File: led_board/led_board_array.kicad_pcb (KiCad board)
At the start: 2 copper layers, 87.6 x 84 mm, 144 parts, among them J1 Conn_01x03, J2 Conn_01x02, J3 Conn_01x02, J4 Conn_01x02

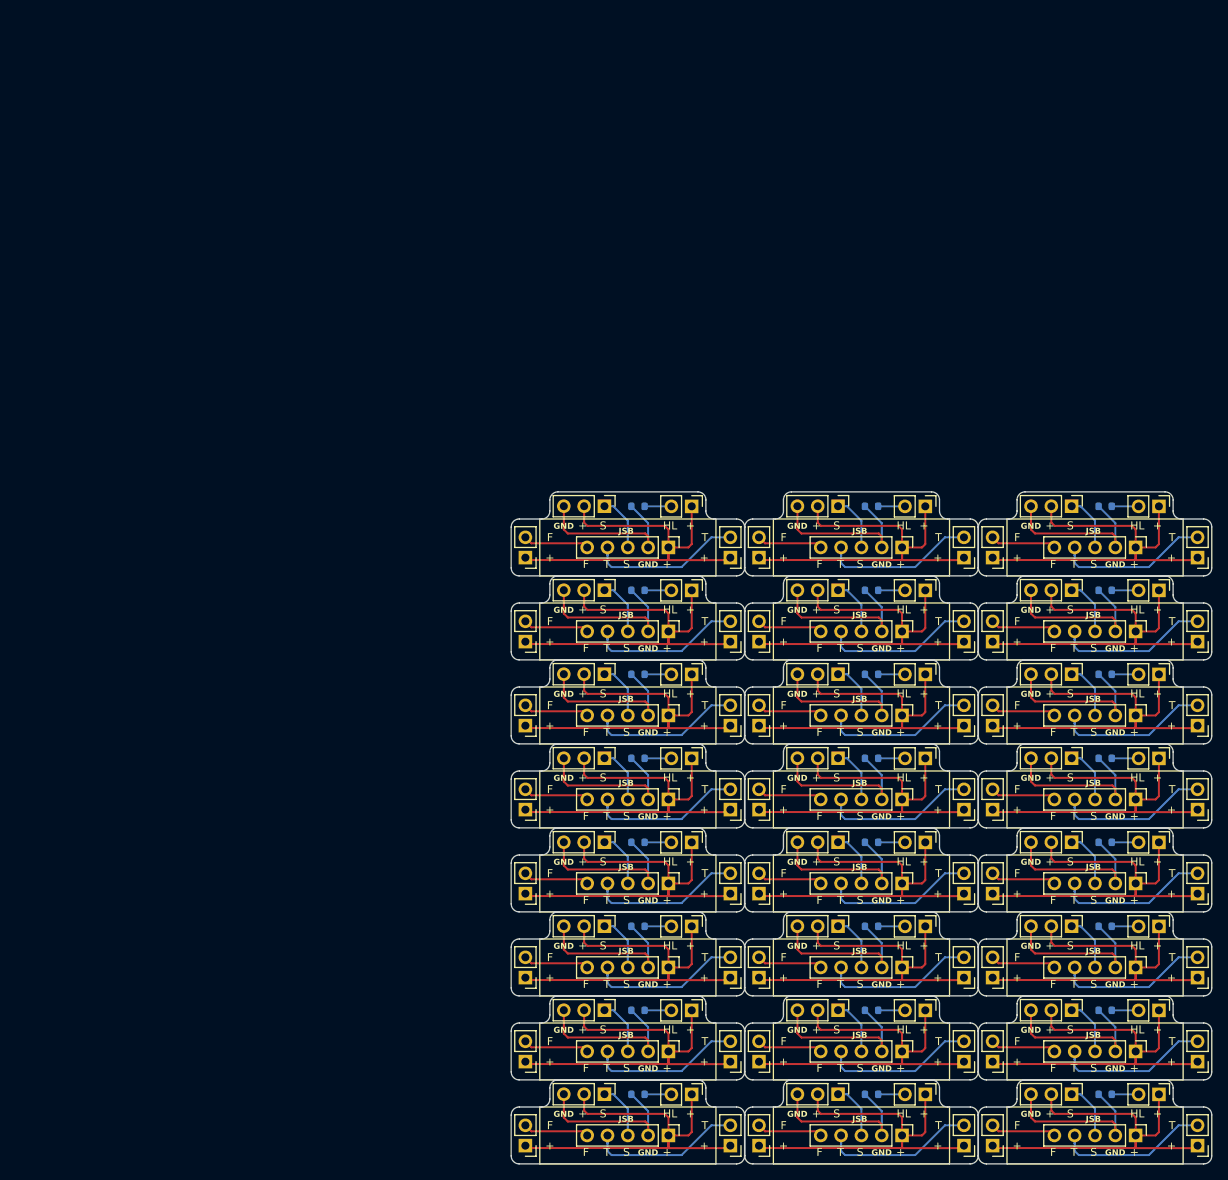
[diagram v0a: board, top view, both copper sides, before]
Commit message: feat: modify logo
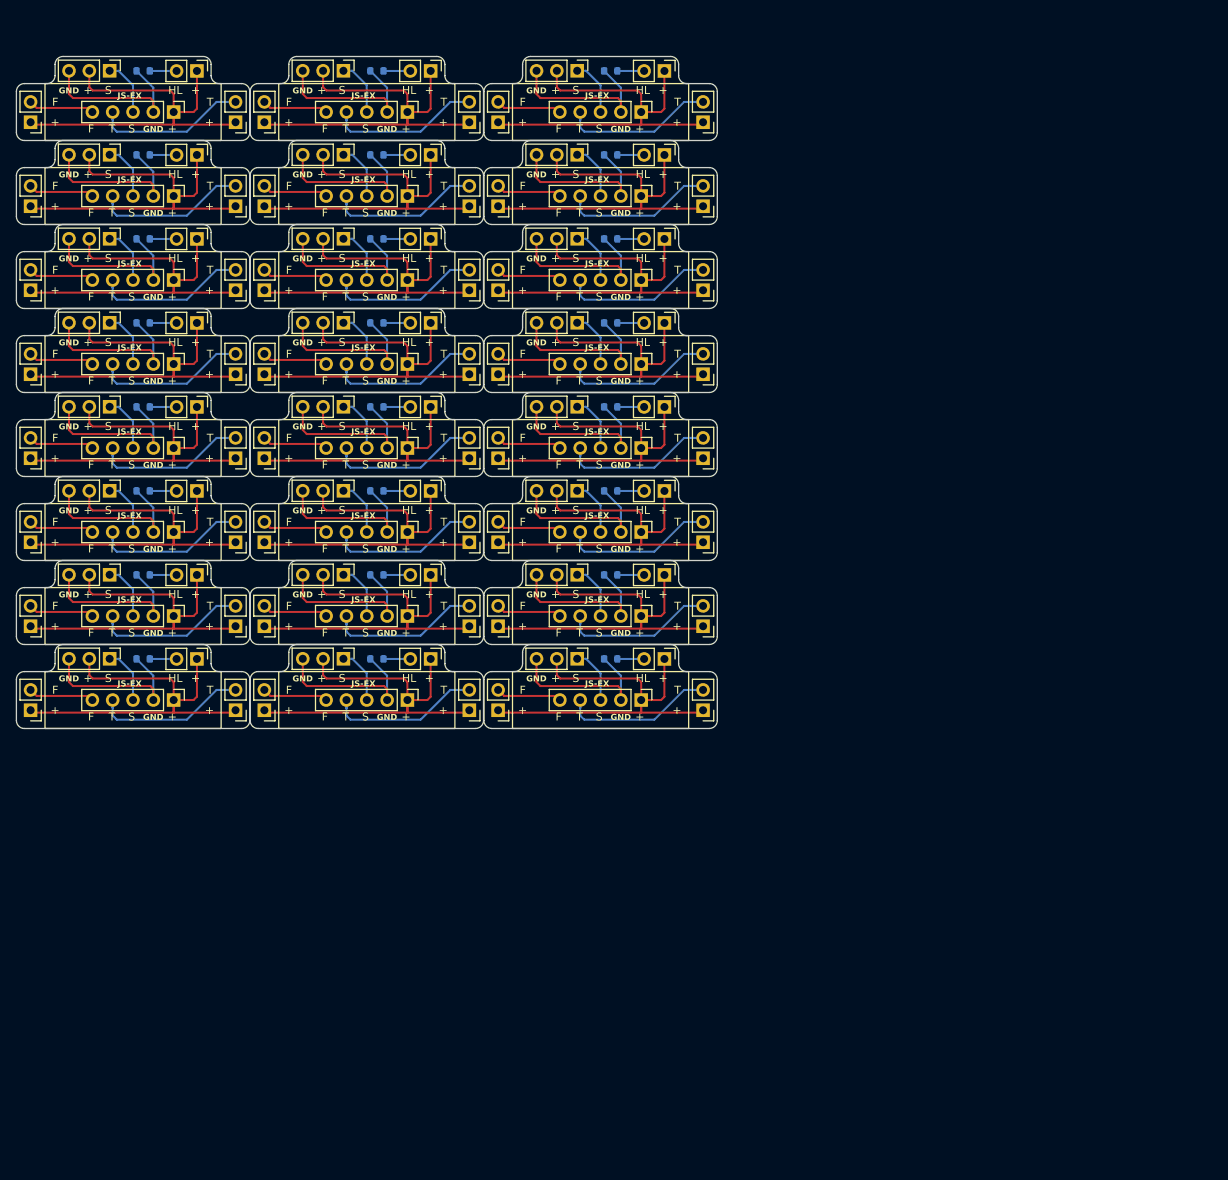
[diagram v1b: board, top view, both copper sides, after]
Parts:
- removed the J1 at (139.3, 150.9)
- removed the J1 at (110.1, 171.9)
- removed the J1 at (168.5, 108.9)
- removed the J1 at (168.5, 171.9)
- removed the J1 at (110.1, 161.4)
- removed the J1 at (110.1, 129.9)
- removed the J1 at (110.1, 98.4)
- removed the J1 at (110.1, 108.9)
- removed the J1 at (139.3, 171.9)
- removed the J1 at (168.5, 129.9)
- removed the J1 at (168.5, 150.9)
- removed the J1 at (110.1, 150.9)
- removed the J1 at (168.5, 140.4)
- removed the J1 at (110.1, 140.4)
- removed the J1 at (139.3, 129.9)
- removed the J1 at (139.3, 108.9)
- removed the J1 at (110.1, 119.4)
- removed the J1 at (139.3, 119.4)
- removed the J1 at (139.3, 98.4)
- removed the J1 at (139.3, 161.4)
- removed the J1 at (168.5, 161.4)
- removed the J1 at (168.5, 98.4)
- removed the J1 at (168.5, 119.4)
- removed the J1 at (139.3, 140.4)
- removed the J2 at (121.0, 140.4)
- removed the J2 at (121.0, 161.4)
- removed the J2 at (121.0, 108.9)
- removed the J2 at (150.2, 150.9)
- removed the J2 at (179.4, 171.9)
- removed the J2 at (150.2, 140.4)
- removed the J2 at (179.4, 119.4)
- removed the J2 at (121.0, 119.4)
- removed the J2 at (121.0, 129.9)
- removed the J2 at (121.0, 150.9)
- removed the J2 at (150.2, 98.4)
- removed the J2 at (179.4, 129.9)
- removed the J2 at (150.2, 161.4)
- removed the J2 at (150.2, 171.9)
- removed the J2 at (179.4, 161.4)
- removed the J2 at (179.4, 98.4)
- removed the J2 at (121.0, 171.9)
- removed the J2 at (121.0, 98.4)
- removed the J2 at (179.4, 140.4)
- removed the J2 at (150.2, 119.4)
- removed the J2 at (179.4, 108.9)
- removed the J2 at (179.4, 150.9)
- removed the J2 at (150.2, 129.9)
- removed the J2 at (150.2, 108.9)
- removed the J3 at (100.2, 136.3)
- removed the J3 at (158.6, 136.3)
- removed the J3 at (129.4, 157.3)
- removed the J3 at (158.6, 125.8)
- removed the J3 at (129.4, 167.8)
- removed the J3 at (158.6, 167.8)
- removed the J3 at (100.2, 167.8)
- removed the J3 at (100.2, 146.8)
- removed the J3 at (129.4, 104.8)
- removed the J3 at (158.6, 157.3)
- removed the J3 at (158.6, 146.8)
- removed the J3 at (129.4, 178.3)
- removed the J3 at (158.6, 104.8)
- removed the J3 at (129.4, 125.8)
- removed the J3 at (100.2, 157.3)
- removed the J3 at (129.4, 115.3)
- removed the J3 at (129.4, 146.8)
- removed the J3 at (158.6, 115.3)
- removed the J3 at (158.6, 178.3)
- removed the J3 at (100.2, 125.8)
- removed the J3 at (100.2, 115.3)
- removed the J3 at (100.2, 178.3)
- removed the J3 at (100.2, 104.8)
- removed the J3 at (129.4, 136.3)
- removed the J4 at (155.0, 146.8)
- removed the J4 at (155.0, 104.8)
- removed the J4 at (184.2, 115.3)
- removed the J4 at (125.8, 104.8)
- removed the J4 at (125.8, 178.3)
- removed the J4 at (125.8, 125.8)
- removed the J4 at (184.2, 178.3)
- removed the J4 at (155.0, 178.3)
- removed the J4 at (125.8, 115.3)
- removed the J4 at (184.2, 104.8)
- removed the J4 at (184.2, 157.3)
- removed the J4 at (155.0, 167.8)
- removed the J4 at (125.8, 157.3)
- removed the J4 at (155.0, 115.3)
- removed the J4 at (155.0, 157.3)
- removed the J4 at (184.2, 167.8)
- removed the J4 at (125.8, 146.8)
- removed the J4 at (125.8, 136.3)
- removed the J4 at (155.0, 125.8)
- removed the J4 at (184.2, 146.8)
- removed the J4 at (184.2, 136.3)
- removed the J4 at (125.8, 167.8)
- removed the J4 at (155.0, 136.3)
- removed the J4 at (184.2, 125.8)
- removed the JSB1 at (118.1, 135.1)
- removed the JSB1 at (118.1, 156.1)
- removed the JSB1 at (118.1, 177.1)
- removed the JSB1 at (118.1, 124.6)
- removed the JSB1 at (176.5, 135.1)
- removed the JSB1 at (147.3, 156.1)
- removed the JSB1 at (118.1, 145.6)
- removed the JSB1 at (176.5, 156.1)
- removed the JSB1 at (147.3, 166.6)
- removed the JSB1 at (118.1, 114.1)
- removed the JSB1 at (176.5, 114.1)
- removed the JSB1 at (147.3, 124.6)
- removed the JSB1 at (176.5, 177.1)
- removed the JSB1 at (147.3, 177.1)
- removed the JSB1 at (118.1, 166.6)
- removed the JSB1 at (147.3, 103.6)
- removed the JSB1 at (147.3, 135.1)
- removed the JSB1 at (147.3, 114.1)
- removed the JSB1 at (176.5, 103.6)
- removed the JSB1 at (176.5, 124.6)
- removed the JSB1 at (176.5, 145.6)
- removed the JSB1 at (147.3, 145.6)
- removed the JSB1 at (176.5, 166.6)
- removed the JSB1 at (118.1, 103.6)
- removed the R1 at (172.7, 119.4)
- removed the R1 at (172.7, 140.4)
- removed the R1 at (172.7, 171.9)
- removed the R1 at (114.3, 171.9)
- removed the R1 at (143.5, 108.9)
- removed the R1 at (114.3, 119.4)
- removed the R1 at (114.3, 161.4)
- removed the R1 at (172.7, 108.9)
- removed the R1 at (114.3, 140.4)
- removed the R1 at (172.7, 98.4)
- removed the R1 at (143.5, 129.9)
- removed the R1 at (114.3, 129.9)
- removed the R1 at (143.5, 161.4)
- removed the R1 at (143.5, 119.4)
- removed the R1 at (143.5, 140.4)
- removed the R1 at (143.5, 98.4)
- removed the R1 at (143.5, 150.9)
- removed the R1 at (143.5, 171.9)
- removed the R1 at (172.7, 150.9)
- removed the R1 at (172.7, 161.4)
- removed the R1 at (114.3, 108.9)
- removed the R1 at (172.7, 129.9)
- removed the R1 at (114.3, 150.9)
- removed the R1 at (114.3, 98.4)
- added J1: Conn_01x03, Connector_PinHeader_2.54mm:PinHeader_1x03_P2.54mm_Vertical, F.Cu at (48.2, 44.0)
- added J1: Conn_01x03, Connector_PinHeader_2.54mm:PinHeader_1x03_P2.54mm_Vertical, F.Cu at (48.2, 117.5)
- added J1: Conn_01x03, Connector_PinHeader_2.54mm:PinHeader_1x03_P2.54mm_Vertical, F.Cu at (48.2, 75.5)
- added J1: Conn_01x03, Connector_PinHeader_2.54mm:PinHeader_1x03_P2.54mm_Vertical, F.Cu at (106.7, 65.0)
- added J1: Conn_01x03, Connector_PinHeader_2.54mm:PinHeader_1x03_P2.54mm_Vertical, F.Cu at (77.5, 54.5)
- added J1: Conn_01x03, Connector_PinHeader_2.54mm:PinHeader_1x03_P2.54mm_Vertical, F.Cu at (48.2, 54.5)
- added J1: Conn_01x03, Connector_PinHeader_2.54mm:PinHeader_1x03_P2.54mm_Vertical, F.Cu at (106.7, 44.0)
- added J1: Conn_01x03, Connector_PinHeader_2.54mm:PinHeader_1x03_P2.54mm_Vertical, F.Cu at (106.7, 96.5)
- added J1: Conn_01x03, Connector_PinHeader_2.54mm:PinHeader_1x03_P2.54mm_Vertical, F.Cu at (48.2, 65.0)
- added J1: Conn_01x03, Connector_PinHeader_2.54mm:PinHeader_1x03_P2.54mm_Vertical, F.Cu at (77.5, 117.5)
- added J1: Conn_01x03, Connector_PinHeader_2.54mm:PinHeader_1x03_P2.54mm_Vertical, F.Cu at (106.7, 54.5)
- added J1: Conn_01x03, Connector_PinHeader_2.54mm:PinHeader_1x03_P2.54mm_Vertical, F.Cu at (48.2, 107.0)
- added J1: Conn_01x03, Connector_PinHeader_2.54mm:PinHeader_1x03_P2.54mm_Vertical, F.Cu at (77.5, 96.5)
- added J1: Conn_01x03, Connector_PinHeader_2.54mm:PinHeader_1x03_P2.54mm_Vertical, F.Cu at (106.7, 107.0)
- added J1: Conn_01x03, Connector_PinHeader_2.54mm:PinHeader_1x03_P2.54mm_Vertical, F.Cu at (48.2, 96.5)
- added J1: Conn_01x03, Connector_PinHeader_2.54mm:PinHeader_1x03_P2.54mm_Vertical, F.Cu at (77.5, 75.5)
- added J1: Conn_01x03, Connector_PinHeader_2.54mm:PinHeader_1x03_P2.54mm_Vertical, F.Cu at (77.5, 86.0)
- added J1: Conn_01x03, Connector_PinHeader_2.54mm:PinHeader_1x03_P2.54mm_Vertical, F.Cu at (77.5, 107.0)
- added J1: Conn_01x03, Connector_PinHeader_2.54mm:PinHeader_1x03_P2.54mm_Vertical, F.Cu at (77.5, 65.0)
- added J1: Conn_01x03, Connector_PinHeader_2.54mm:PinHeader_1x03_P2.54mm_Vertical, F.Cu at (106.7, 117.5)
- added J1: Conn_01x03, Connector_PinHeader_2.54mm:PinHeader_1x03_P2.54mm_Vertical, F.Cu at (77.5, 44.0)
- added J1: Conn_01x03, Connector_PinHeader_2.54mm:PinHeader_1x03_P2.54mm_Vertical, F.Cu at (106.7, 86.0)
- added J1: Conn_01x03, Connector_PinHeader_2.54mm:PinHeader_1x03_P2.54mm_Vertical, F.Cu at (106.7, 75.5)
- added J1: Conn_01x03, Connector_PinHeader_2.54mm:PinHeader_1x03_P2.54mm_Vertical, F.Cu at (48.2, 86.0)
- added J2: Conn_01x02, Connector_PinHeader_2.54mm:PinHeader_1x02_P2.54mm_Vertical, F.Cu at (59.1, 65.0)
- added J2: Conn_01x02, Connector_PinHeader_2.54mm:PinHeader_1x02_P2.54mm_Vertical, F.Cu at (88.4, 44.0)
- added J2: Conn_01x02, Connector_PinHeader_2.54mm:PinHeader_1x02_P2.54mm_Vertical, F.Cu at (117.6, 65.0)
- added J2: Conn_01x02, Connector_PinHeader_2.54mm:PinHeader_1x02_P2.54mm_Vertical, F.Cu at (59.1, 117.5)
- added J2: Conn_01x02, Connector_PinHeader_2.54mm:PinHeader_1x02_P2.54mm_Vertical, F.Cu at (117.6, 107.0)
- added J2: Conn_01x02, Connector_PinHeader_2.54mm:PinHeader_1x02_P2.54mm_Vertical, F.Cu at (117.6, 44.0)
- added J2: Conn_01x02, Connector_PinHeader_2.54mm:PinHeader_1x02_P2.54mm_Vertical, F.Cu at (88.4, 107.0)
- added J2: Conn_01x02, Connector_PinHeader_2.54mm:PinHeader_1x02_P2.54mm_Vertical, F.Cu at (59.1, 44.0)
- added J2: Conn_01x02, Connector_PinHeader_2.54mm:PinHeader_1x02_P2.54mm_Vertical, F.Cu at (88.4, 75.5)
- added J2: Conn_01x02, Connector_PinHeader_2.54mm:PinHeader_1x02_P2.54mm_Vertical, F.Cu at (88.4, 117.5)
- added J2: Conn_01x02, Connector_PinHeader_2.54mm:PinHeader_1x02_P2.54mm_Vertical, F.Cu at (88.4, 96.5)
- added J2: Conn_01x02, Connector_PinHeader_2.54mm:PinHeader_1x02_P2.54mm_Vertical, F.Cu at (88.4, 54.5)
- added J2: Conn_01x02, Connector_PinHeader_2.54mm:PinHeader_1x02_P2.54mm_Vertical, F.Cu at (59.1, 107.0)
- added J2: Conn_01x02, Connector_PinHeader_2.54mm:PinHeader_1x02_P2.54mm_Vertical, F.Cu at (117.6, 117.5)
- added J2: Conn_01x02, Connector_PinHeader_2.54mm:PinHeader_1x02_P2.54mm_Vertical, F.Cu at (117.6, 75.5)
- added J2: Conn_01x02, Connector_PinHeader_2.54mm:PinHeader_1x02_P2.54mm_Vertical, F.Cu at (59.1, 96.5)
- added J2: Conn_01x02, Connector_PinHeader_2.54mm:PinHeader_1x02_P2.54mm_Vertical, F.Cu at (117.6, 86.0)
- added J2: Conn_01x02, Connector_PinHeader_2.54mm:PinHeader_1x02_P2.54mm_Vertical, F.Cu at (88.4, 65.0)
- added J2: Conn_01x02, Connector_PinHeader_2.54mm:PinHeader_1x02_P2.54mm_Vertical, F.Cu at (117.6, 96.5)
- added J2: Conn_01x02, Connector_PinHeader_2.54mm:PinHeader_1x02_P2.54mm_Vertical, F.Cu at (117.6, 54.5)
- added J2: Conn_01x02, Connector_PinHeader_2.54mm:PinHeader_1x02_P2.54mm_Vertical, F.Cu at (88.4, 86.0)
- added J2: Conn_01x02, Connector_PinHeader_2.54mm:PinHeader_1x02_P2.54mm_Vertical, F.Cu at (59.1, 75.5)
- added J2: Conn_01x02, Connector_PinHeader_2.54mm:PinHeader_1x02_P2.54mm_Vertical, F.Cu at (59.1, 54.5)
- added J2: Conn_01x02, Connector_PinHeader_2.54mm:PinHeader_1x02_P2.54mm_Vertical, F.Cu at (59.1, 86.0)
- added J3: Conn_01x02, Connector_PinHeader_2.54mm:PinHeader_1x02_P2.54mm_Vertical, F.Cu at (96.8, 113.4)
- added J3: Conn_01x02, Connector_PinHeader_2.54mm:PinHeader_1x02_P2.54mm_Vertical, F.Cu at (38.4, 71.4)
- added J3: Conn_01x02, Connector_PinHeader_2.54mm:PinHeader_1x02_P2.54mm_Vertical, F.Cu at (96.8, 102.9)
- added J3: Conn_01x02, Connector_PinHeader_2.54mm:PinHeader_1x02_P2.54mm_Vertical, F.Cu at (67.6, 123.9)
- added J3: Conn_01x02, Connector_PinHeader_2.54mm:PinHeader_1x02_P2.54mm_Vertical, F.Cu at (96.8, 92.4)
- added J3: Conn_01x02, Connector_PinHeader_2.54mm:PinHeader_1x02_P2.54mm_Vertical, F.Cu at (67.6, 71.4)
- added J3: Conn_01x02, Connector_PinHeader_2.54mm:PinHeader_1x02_P2.54mm_Vertical, F.Cu at (96.8, 81.9)
- added J3: Conn_01x02, Connector_PinHeader_2.54mm:PinHeader_1x02_P2.54mm_Vertical, F.Cu at (67.6, 92.4)
- added J3: Conn_01x02, Connector_PinHeader_2.54mm:PinHeader_1x02_P2.54mm_Vertical, F.Cu at (67.6, 81.9)
- added J3: Conn_01x02, Connector_PinHeader_2.54mm:PinHeader_1x02_P2.54mm_Vertical, F.Cu at (38.4, 92.4)
- added J3: Conn_01x02, Connector_PinHeader_2.54mm:PinHeader_1x02_P2.54mm_Vertical, F.Cu at (96.8, 123.9)
- added J3: Conn_01x02, Connector_PinHeader_2.54mm:PinHeader_1x02_P2.54mm_Vertical, F.Cu at (67.6, 60.9)
- added J3: Conn_01x02, Connector_PinHeader_2.54mm:PinHeader_1x02_P2.54mm_Vertical, F.Cu at (67.6, 113.4)
- added J3: Conn_01x02, Connector_PinHeader_2.54mm:PinHeader_1x02_P2.54mm_Vertical, F.Cu at (38.4, 102.9)
- added J3: Conn_01x02, Connector_PinHeader_2.54mm:PinHeader_1x02_P2.54mm_Vertical, F.Cu at (96.8, 50.4)
- added J3: Conn_01x02, Connector_PinHeader_2.54mm:PinHeader_1x02_P2.54mm_Vertical, F.Cu at (67.6, 102.9)
- added J3: Conn_01x02, Connector_PinHeader_2.54mm:PinHeader_1x02_P2.54mm_Vertical, F.Cu at (38.4, 113.4)
- added J3: Conn_01x02, Connector_PinHeader_2.54mm:PinHeader_1x02_P2.54mm_Vertical, F.Cu at (96.8, 71.4)
- added J3: Conn_01x02, Connector_PinHeader_2.54mm:PinHeader_1x02_P2.54mm_Vertical, F.Cu at (67.6, 50.4)
- added J3: Conn_01x02, Connector_PinHeader_2.54mm:PinHeader_1x02_P2.54mm_Vertical, F.Cu at (96.8, 60.9)
- added J3: Conn_01x02, Connector_PinHeader_2.54mm:PinHeader_1x02_P2.54mm_Vertical, F.Cu at (38.4, 123.9)
- added J3: Conn_01x02, Connector_PinHeader_2.54mm:PinHeader_1x02_P2.54mm_Vertical, F.Cu at (38.4, 50.4)
- added J3: Conn_01x02, Connector_PinHeader_2.54mm:PinHeader_1x02_P2.54mm_Vertical, F.Cu at (38.4, 81.9)
- added J3: Conn_01x02, Connector_PinHeader_2.54mm:PinHeader_1x02_P2.54mm_Vertical, F.Cu at (38.4, 60.9)
- added J4: Conn_01x02, Connector_PinHeader_2.54mm:PinHeader_1x02_P2.54mm_Vertical, F.Cu at (122.4, 81.9)
- added J4: Conn_01x02, Connector_PinHeader_2.54mm:PinHeader_1x02_P2.54mm_Vertical, F.Cu at (122.4, 71.4)
- added J4: Conn_01x02, Connector_PinHeader_2.54mm:PinHeader_1x02_P2.54mm_Vertical, F.Cu at (64.0, 123.9)
- added J4: Conn_01x02, Connector_PinHeader_2.54mm:PinHeader_1x02_P2.54mm_Vertical, F.Cu at (122.4, 50.4)
- added J4: Conn_01x02, Connector_PinHeader_2.54mm:PinHeader_1x02_P2.54mm_Vertical, F.Cu at (93.2, 123.9)
- added J4: Conn_01x02, Connector_PinHeader_2.54mm:PinHeader_1x02_P2.54mm_Vertical, F.Cu at (64.0, 102.9)
- added J4: Conn_01x02, Connector_PinHeader_2.54mm:PinHeader_1x02_P2.54mm_Vertical, F.Cu at (93.2, 71.4)
- added J4: Conn_01x02, Connector_PinHeader_2.54mm:PinHeader_1x02_P2.54mm_Vertical, F.Cu at (64.0, 60.9)
- added J4: Conn_01x02, Connector_PinHeader_2.54mm:PinHeader_1x02_P2.54mm_Vertical, F.Cu at (122.4, 92.4)
- added J4: Conn_01x02, Connector_PinHeader_2.54mm:PinHeader_1x02_P2.54mm_Vertical, F.Cu at (93.2, 50.4)
- added J4: Conn_01x02, Connector_PinHeader_2.54mm:PinHeader_1x02_P2.54mm_Vertical, F.Cu at (122.4, 60.9)
- added J4: Conn_01x02, Connector_PinHeader_2.54mm:PinHeader_1x02_P2.54mm_Vertical, F.Cu at (122.4, 102.9)
- added J4: Conn_01x02, Connector_PinHeader_2.54mm:PinHeader_1x02_P2.54mm_Vertical, F.Cu at (93.2, 113.4)
- added J4: Conn_01x02, Connector_PinHeader_2.54mm:PinHeader_1x02_P2.54mm_Vertical, F.Cu at (122.4, 113.4)
- added J4: Conn_01x02, Connector_PinHeader_2.54mm:PinHeader_1x02_P2.54mm_Vertical, F.Cu at (64.0, 71.4)
- added J4: Conn_01x02, Connector_PinHeader_2.54mm:PinHeader_1x02_P2.54mm_Vertical, F.Cu at (64.0, 113.4)
- added J4: Conn_01x02, Connector_PinHeader_2.54mm:PinHeader_1x02_P2.54mm_Vertical, F.Cu at (64.0, 92.4)
- added J4: Conn_01x02, Connector_PinHeader_2.54mm:PinHeader_1x02_P2.54mm_Vertical, F.Cu at (64.0, 50.4)
- added J4: Conn_01x02, Connector_PinHeader_2.54mm:PinHeader_1x02_P2.54mm_Vertical, F.Cu at (93.2, 92.4)
- added J4: Conn_01x02, Connector_PinHeader_2.54mm:PinHeader_1x02_P2.54mm_Vertical, F.Cu at (93.2, 81.9)
- added J4: Conn_01x02, Connector_PinHeader_2.54mm:PinHeader_1x02_P2.54mm_Vertical, F.Cu at (93.2, 60.9)
- added J4: Conn_01x02, Connector_PinHeader_2.54mm:PinHeader_1x02_P2.54mm_Vertical, F.Cu at (64.0, 81.9)
- added J4: Conn_01x02, Connector_PinHeader_2.54mm:PinHeader_1x02_P2.54mm_Vertical, F.Cu at (93.2, 102.9)
- added J4: Conn_01x02, Connector_PinHeader_2.54mm:PinHeader_1x02_P2.54mm_Vertical, F.Cu at (122.4, 123.9)
- added JSB1: Conn_01x05, Connector_PinHeader_2.54mm:PinHeader_1x05_P2.54mm_Vertical, F.Cu at (114.7, 59.6)
- added JSB1: Conn_01x05, Connector_PinHeader_2.54mm:PinHeader_1x05_P2.54mm_Vertical, F.Cu at (85.5, 101.6)
- added JSB1: Conn_01x05, Connector_PinHeader_2.54mm:PinHeader_1x05_P2.54mm_Vertical, F.Cu at (114.7, 91.1)
- added JSB1: Conn_01x05, Connector_PinHeader_2.54mm:PinHeader_1x05_P2.54mm_Vertical, F.Cu at (85.5, 122.6)
- added JSB1: Conn_01x05, Connector_PinHeader_2.54mm:PinHeader_1x05_P2.54mm_Vertical, F.Cu at (85.5, 70.1)
- added JSB1: Conn_01x05, Connector_PinHeader_2.54mm:PinHeader_1x05_P2.54mm_Vertical, F.Cu at (56.2, 112.1)
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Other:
- outline, holes or cut-outs redrawn
- board text added: "JS-EX"
- board text removed: "JSB"

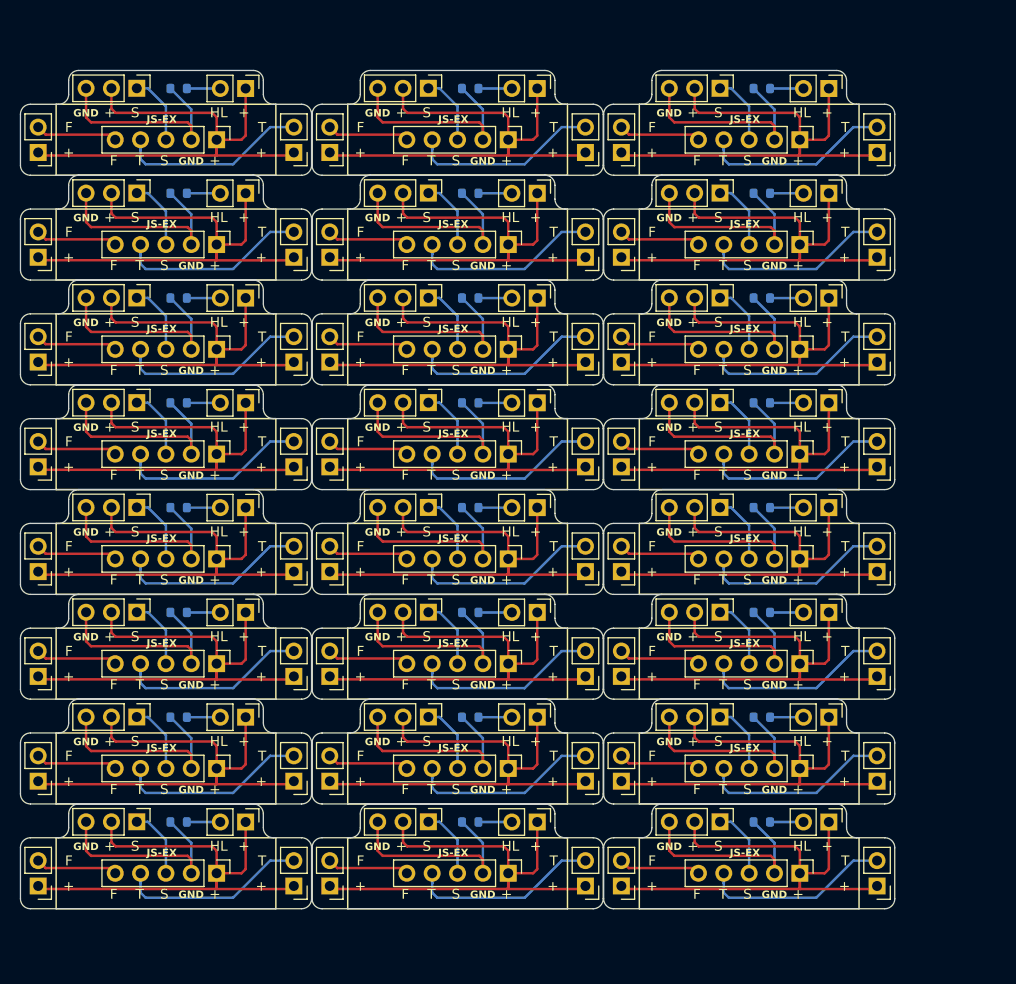
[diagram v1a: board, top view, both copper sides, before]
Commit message: feat(led_board): update array
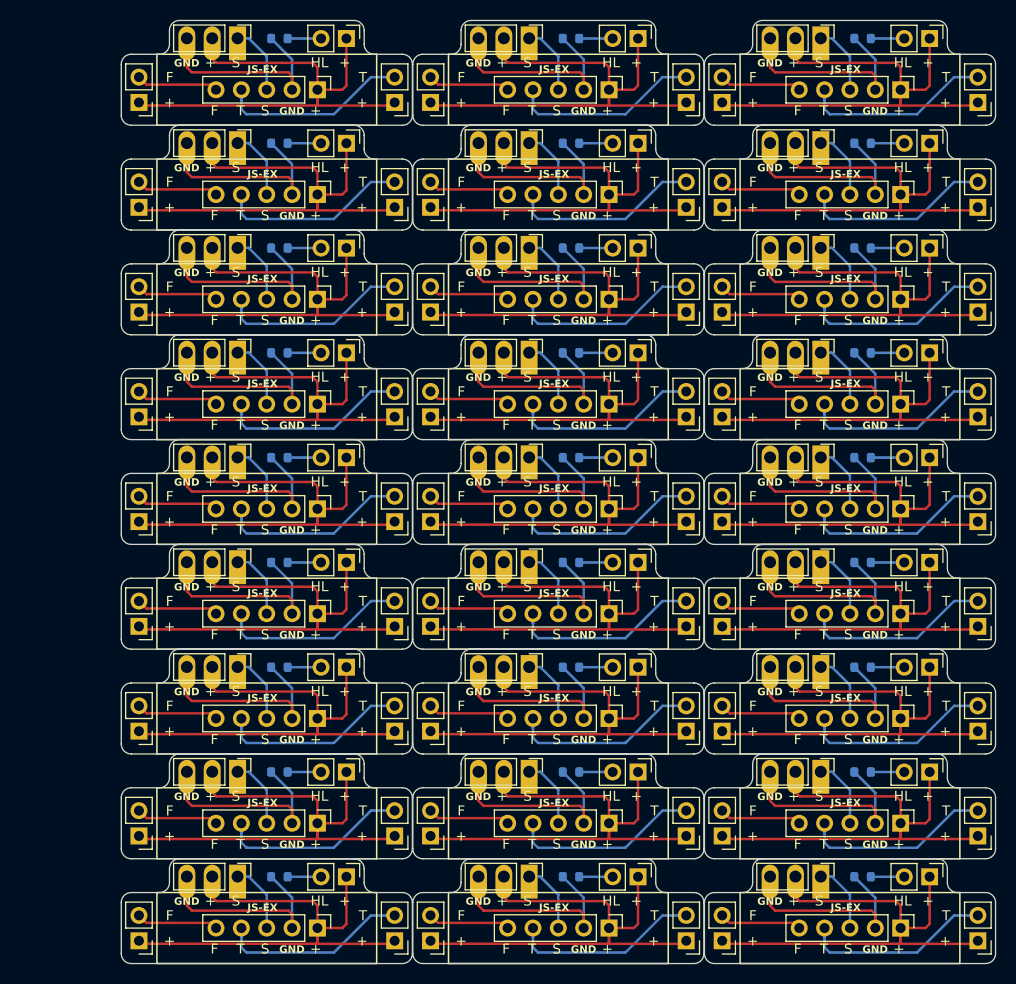
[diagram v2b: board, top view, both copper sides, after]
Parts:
- removed the J1 at (48.2, 44.0)
- removed the J1 at (48.2, 117.5)
- removed the J1 at (48.2, 75.5)
- removed the J1 at (106.7, 65.0)
- removed the J1 at (77.5, 54.5)
- removed the J1 at (48.2, 54.5)
- removed the J1 at (106.7, 44.0)
- removed the J1 at (106.7, 96.5)
- removed the J1 at (48.2, 65.0)
- removed the J1 at (77.5, 117.5)
- removed the J1 at (106.7, 54.5)
- removed the J1 at (48.2, 107.0)
- removed the J1 at (77.5, 96.5)
- removed the J1 at (106.7, 107.0)
- removed the J1 at (48.2, 96.5)
- removed the J1 at (77.5, 75.5)
- removed the J1 at (77.5, 86.0)
- removed the J1 at (77.5, 107.0)
- removed the J1 at (77.5, 65.0)
- removed the J1 at (106.7, 117.5)
- removed the J1 at (77.5, 44.0)
- removed the J1 at (106.7, 86.0)
- removed the J1 at (106.7, 75.5)
- removed the J1 at (48.2, 86.0)
- removed the J2 at (59.1, 65.0)
- removed the J2 at (88.4, 44.0)
- removed the J2 at (117.6, 65.0)
- removed the J2 at (59.1, 117.5)
- removed the J2 at (117.6, 107.0)
- removed the J2 at (117.6, 44.0)
- removed the J2 at (88.4, 107.0)
- removed the J2 at (59.1, 44.0)
- removed the J2 at (88.4, 75.5)
- removed the J2 at (88.4, 117.5)
- removed the J2 at (88.4, 96.5)
- removed the J2 at (88.4, 54.5)
- removed the J2 at (59.1, 107.0)
- removed the J2 at (117.6, 117.5)
- removed the J2 at (117.6, 75.5)
- removed the J2 at (59.1, 96.5)
- removed the J2 at (117.6, 86.0)
- removed the J2 at (88.4, 65.0)
- removed the J2 at (117.6, 96.5)
- removed the J2 at (117.6, 54.5)
- removed the J2 at (88.4, 86.0)
- removed the J2 at (59.1, 75.5)
- removed the J2 at (59.1, 54.5)
- removed the J2 at (59.1, 86.0)
- removed the J3 at (96.8, 113.4)
- removed the J3 at (38.4, 71.4)
- removed the J3 at (96.8, 102.9)
- removed the J3 at (67.6, 123.9)
- removed the J3 at (96.8, 92.4)
- removed the J3 at (67.6, 71.4)
- removed the J3 at (96.8, 81.9)
- removed the J3 at (67.6, 92.4)
- removed the J3 at (67.6, 81.9)
- removed the J3 at (38.4, 92.4)
- removed the J3 at (96.8, 123.9)
- removed the J3 at (67.6, 60.9)
- removed the J3 at (67.6, 113.4)
- removed the J3 at (38.4, 102.9)
- removed the J3 at (96.8, 50.4)
- removed the J3 at (67.6, 102.9)
- removed the J3 at (38.4, 113.4)
- removed the J3 at (96.8, 71.4)
- removed the J3 at (67.6, 50.4)
- removed the J3 at (96.8, 60.9)
- removed the J3 at (38.4, 123.9)
- removed the J3 at (38.4, 50.4)
- removed the J3 at (38.4, 81.9)
- removed the J3 at (38.4, 60.9)
- removed the J4 at (122.4, 81.9)
- removed the J4 at (122.4, 71.4)
- removed the J4 at (64.0, 123.9)
- removed the J4 at (122.4, 50.4)
- removed the J4 at (93.2, 123.9)
- removed the J4 at (64.0, 102.9)
- removed the J4 at (93.2, 71.4)
- removed the J4 at (64.0, 60.9)
- removed the J4 at (122.4, 92.4)
- removed the J4 at (93.2, 50.4)
- removed the J4 at (122.4, 60.9)
- removed the J4 at (122.4, 102.9)
- removed the J4 at (93.2, 113.4)
- removed the J4 at (122.4, 113.4)
- removed the J4 at (64.0, 71.4)
- removed the J4 at (64.0, 113.4)
- removed the J4 at (64.0, 92.4)
- removed the J4 at (64.0, 50.4)
- removed the J4 at (93.2, 92.4)
- removed the J4 at (93.2, 81.9)
- removed the J4 at (93.2, 60.9)
- removed the J4 at (64.0, 81.9)
- removed the J4 at (93.2, 102.9)
- removed the J4 at (122.4, 123.9)
- removed the JSB1 at (114.7, 59.6)
- removed the JSB1 at (85.5, 101.6)
- removed the JSB1 at (114.7, 91.1)
- removed the JSB1 at (85.5, 122.6)
- removed the JSB1 at (85.5, 70.1)
- removed the JSB1 at (56.2, 112.1)
- removed the JSB1 at (114.7, 80.6)
- removed the JSB1 at (114.7, 101.6)
- removed the JSB1 at (114.7, 70.1)
- removed the JSB1 at (56.2, 70.1)
- removed the JSB1 at (85.5, 91.1)
- removed the JSB1 at (56.2, 91.1)
- removed the JSB1 at (56.2, 80.6)
- removed the JSB1 at (56.2, 49.1)
- removed the JSB1 at (56.2, 59.6)
- removed the JSB1 at (85.5, 112.1)
- removed the JSB1 at (85.5, 59.6)
- removed the JSB1 at (56.2, 122.6)
- removed the JSB1 at (85.5, 80.6)
- removed the JSB1 at (85.5, 49.1)
- removed the JSB1 at (114.7, 122.6)
- removed the JSB1 at (56.2, 101.6)
- removed the JSB1 at (114.7, 112.1)
- removed the JSB1 at (114.7, 49.1)
- removed the R1 at (52.4, 44.0)
- removed the R1 at (52.4, 117.5)
- removed the R1 at (52.4, 65.0)
- removed the R1 at (52.4, 54.5)
- removed the R1 at (110.9, 54.5)
- removed the R1 at (81.7, 96.5)
- removed the R1 at (52.4, 107.0)
- removed the R1 at (52.4, 96.5)
- removed the R1 at (110.9, 107.0)
- removed the R1 at (81.7, 107.0)
- removed the R1 at (110.9, 117.5)
- removed the R1 at (110.9, 65.0)
- removed the R1 at (110.9, 86.0)
- removed the R1 at (81.7, 117.5)
- removed the R1 at (81.7, 86.0)
- removed the R1 at (110.9, 44.0)
- removed the R1 at (110.9, 75.5)
- removed the R1 at (110.9, 96.5)
- removed the R1 at (81.7, 75.5)
- removed the R1 at (81.7, 65.0)
- removed the R1 at (81.7, 54.5)
- removed the R1 at (52.4, 86.0)
- removed the R1 at (81.7, 44.0)
- removed the R1 at (52.4, 75.5)
- added J1: Conn_01x03, Connector_PinHeader_2.54mm:PinHeader_1x03_P2.54mm_Vertical, F.Cu at (87.6, 81.0)
- added J1: Conn_01x03, Connector_PinHeader_2.54mm:PinHeader_1x03_P2.54mm_Vertical, F.Cu at (58.3, 91.5)
- added J1: Conn_01x03, Connector_PinHeader_2.54mm:PinHeader_1x03_P2.54mm_Vertical, F.Cu at (116.8, 91.5)
- added J1: Conn_01x03, Connector_PinHeader_2.54mm:PinHeader_1x03_P2.54mm_Vertical, F.Cu at (58.3, 39.0)
- added J1: Conn_01x03, Connector_PinHeader_2.54mm:PinHeader_1x03_P2.54mm_Vertical, F.Cu at (87.6, 60.0)
- added J1: Conn_01x03, Connector_PinHeader_2.54mm:PinHeader_1x03_P2.54mm_Vertical, F.Cu at (58.3, 70.5)
- added J1: Conn_01x03, Connector_PinHeader_2.54mm:PinHeader_1x03_P2.54mm_Vertical, F.Cu at (116.8, 81.0)
- added J1: Conn_01x03, Connector_PinHeader_2.54mm:PinHeader_1x03_P2.54mm_Vertical, F.Cu at (116.8, 70.5)
- added J1: Conn_01x03, Connector_PinHeader_2.54mm:PinHeader_1x03_P2.54mm_Vertical, F.Cu at (87.6, 123.0)
- added J1: Conn_01x03, Connector_PinHeader_2.54mm:PinHeader_1x03_P2.54mm_Vertical, F.Cu at (58.3, 112.5)
- added J1: Conn_01x03, Connector_PinHeader_2.54mm:PinHeader_1x03_P2.54mm_Vertical, F.Cu at (116.8, 60.0)
- added J1: Conn_01x03, Connector_PinHeader_2.54mm:PinHeader_1x03_P2.54mm_Vertical, F.Cu at (87.6, 49.5)
- added J1: Conn_01x03, Connector_PinHeader_2.54mm:PinHeader_1x03_P2.54mm_Vertical, F.Cu at (116.8, 112.5)
- added J1: Conn_01x03, Connector_PinHeader_2.54mm:PinHeader_1x03_P2.54mm_Vertical, F.Cu at (58.3, 49.5)
- added J1: Conn_01x03, Connector_PinHeader_2.54mm:PinHeader_1x03_P2.54mm_Vertical, F.Cu at (116.8, 123.0)
- added J1: Conn_01x03, Connector_PinHeader_2.54mm:PinHeader_1x03_P2.54mm_Vertical, F.Cu at (58.3, 60.0)
- added J1: Conn_01x03, Connector_PinHeader_2.54mm:PinHeader_1x03_P2.54mm_Vertical, F.Cu at (87.6, 39.0)
- added J1: Conn_01x03, Connector_PinHeader_2.54mm:PinHeader_1x03_P2.54mm_Vertical, F.Cu at (58.3, 81.0)
- added J1: Conn_01x03, Connector_PinHeader_2.54mm:PinHeader_1x03_P2.54mm_Vertical, F.Cu at (116.8, 49.5)
- added J1: Conn_01x03, Connector_PinHeader_2.54mm:PinHeader_1x03_P2.54mm_Vertical, F.Cu at (87.6, 102.0)
- added J1: Conn_01x03, Connector_PinHeader_2.54mm:PinHeader_1x03_P2.54mm_Vertical, F.Cu at (87.6, 91.5)
- added J1: Conn_01x03, Connector_PinHeader_2.54mm:PinHeader_1x03_P2.54mm_Vertical, F.Cu at (116.8, 102.0)
- added J1: Conn_01x03, Connector_PinHeader_2.54mm:PinHeader_1x03_P2.54mm_Vertical, F.Cu at (58.3, 123.0)
- added J1: Conn_01x03, Connector_PinHeader_2.54mm:PinHeader_1x03_P2.54mm_Vertical, F.Cu at (58.3, 102.0)
- added J1: Conn_01x03, Connector_PinHeader_2.54mm:PinHeader_1x03_P2.54mm_Vertical, F.Cu at (116.8, 39.0)
- added J1: Conn_01x03, Connector_PinHeader_2.54mm:PinHeader_1x03_P2.54mm_Vertical, F.Cu at (87.6, 70.5)
- added J1: Conn_01x03, Connector_PinHeader_2.54mm:PinHeader_1x03_P2.54mm_Vertical, F.Cu at (87.6, 112.5)
- added J2: Conn_01x02, Connector_PinHeader_2.54mm:PinHeader_1x02_P2.54mm_Vertical, F.Cu at (98.5, 112.5)
- added J2: Conn_01x02, Connector_PinHeader_2.54mm:PinHeader_1x02_P2.54mm_Vertical, F.Cu at (98.5, 60.0)
- added J2: Conn_01x02, Connector_PinHeader_2.54mm:PinHeader_1x02_P2.54mm_Vertical, F.Cu at (127.7, 49.5)
- added J2: Conn_01x02, Connector_PinHeader_2.54mm:PinHeader_1x02_P2.54mm_Vertical, F.Cu at (127.7, 91.5)
- added J2: Conn_01x02, Connector_PinHeader_2.54mm:PinHeader_1x02_P2.54mm_Vertical, F.Cu at (98.5, 81.0)
- added J2: Conn_01x02, Connector_PinHeader_2.54mm:PinHeader_1x02_P2.54mm_Vertical, F.Cu at (98.5, 91.5)
- added J2: Conn_01x02, Connector_PinHeader_2.54mm:PinHeader_1x02_P2.54mm_Vertical, F.Cu at (69.2, 112.5)
- added J2: Conn_01x02, Connector_PinHeader_2.54mm:PinHeader_1x02_P2.54mm_Vertical, F.Cu at (69.2, 91.5)
- added J2: Conn_01x02, Connector_PinHeader_2.54mm:PinHeader_1x02_P2.54mm_Vertical, F.Cu at (98.5, 102.0)
- added J2: Conn_01x02, Connector_PinHeader_2.54mm:PinHeader_1x02_P2.54mm_Vertical, F.Cu at (69.2, 60.0)
- added J2: Conn_01x02, Connector_PinHeader_2.54mm:PinHeader_1x02_P2.54mm_Vertical, F.Cu at (69.2, 123.0)
- added J2: Conn_01x02, Connector_PinHeader_2.54mm:PinHeader_1x02_P2.54mm_Vertical, F.Cu at (98.5, 39.0)
- added J2: Conn_01x02, Connector_PinHeader_2.54mm:PinHeader_1x02_P2.54mm_Vertical, F.Cu at (98.5, 49.5)
- added J2: Conn_01x02, Connector_PinHeader_2.54mm:PinHeader_1x02_P2.54mm_Vertical, F.Cu at (127.7, 70.5)
- added J2: Conn_01x02, Connector_PinHeader_2.54mm:PinHeader_1x02_P2.54mm_Vertical, F.Cu at (127.7, 60.0)
- added J2: Conn_01x02, Connector_PinHeader_2.54mm:PinHeader_1x02_P2.54mm_Vertical, F.Cu at (69.2, 39.0)
- added J2: Conn_01x02, Connector_PinHeader_2.54mm:PinHeader_1x02_P2.54mm_Vertical, F.Cu at (127.7, 102.0)
- added J2: Conn_01x02, Connector_PinHeader_2.54mm:PinHeader_1x02_P2.54mm_Vertical, F.Cu at (98.5, 70.5)
- added J2: Conn_01x02, Connector_PinHeader_2.54mm:PinHeader_1x02_P2.54mm_Vertical, F.Cu at (127.7, 39.0)
- added J2: Conn_01x02, Connector_PinHeader_2.54mm:PinHeader_1x02_P2.54mm_Vertical, F.Cu at (127.7, 123.0)
- added J2: Conn_01x02, Connector_PinHeader_2.54mm:PinHeader_1x02_P2.54mm_Vertical, F.Cu at (127.7, 81.0)
- added J2: Conn_01x02, Connector_PinHeader_2.54mm:PinHeader_1x02_P2.54mm_Vertical, F.Cu at (98.5, 123.0)
- added J2: Conn_01x02, Connector_PinHeader_2.54mm:PinHeader_1x02_P2.54mm_Vertical, F.Cu at (69.2, 49.5)
- added J2: Conn_01x02, Connector_PinHeader_2.54mm:PinHeader_1x02_P2.54mm_Vertical, F.Cu at (69.2, 81.0)
- added J2: Conn_01x02, Connector_PinHeader_2.54mm:PinHeader_1x02_P2.54mm_Vertical, F.Cu at (127.7, 112.5)
- added J2: Conn_01x02, Connector_PinHeader_2.54mm:PinHeader_1x02_P2.54mm_Vertical, F.Cu at (69.2, 102.0)
- added J2: Conn_01x02, Connector_PinHeader_2.54mm:PinHeader_1x02_P2.54mm_Vertical, F.Cu at (69.2, 70.5)
- added J3: Conn_01x02, Connector_PinHeader_2.54mm:PinHeader_1x02_P2.54mm_Vertical, F.Cu at (106.9, 76.9)
- added J3: Conn_01x02, Connector_PinHeader_2.54mm:PinHeader_1x02_P2.54mm_Vertical, F.Cu at (48.5, 118.9)
- added J3: Conn_01x02, Connector_PinHeader_2.54mm:PinHeader_1x02_P2.54mm_Vertical, F.Cu at (77.7, 97.9)
- added J3: Conn_01x02, Connector_PinHeader_2.54mm:PinHeader_1x02_P2.54mm_Vertical, F.Cu at (48.5, 76.9)
- added J3: Conn_01x02, Connector_PinHeader_2.54mm:PinHeader_1x02_P2.54mm_Vertical, F.Cu at (106.9, 108.4)
- added J3: Conn_01x02, Connector_PinHeader_2.54mm:PinHeader_1x02_P2.54mm_Vertical, F.Cu at (48.5, 87.4)
- added J3: Conn_01x02, Connector_PinHeader_2.54mm:PinHeader_1x02_P2.54mm_Vertical, F.Cu at (77.7, 87.4)
- added J3: Conn_01x02, Connector_PinHeader_2.54mm:PinHeader_1x02_P2.54mm_Vertical, F.Cu at (77.7, 76.9)
- added J3: Conn_01x02, Connector_PinHeader_2.54mm:PinHeader_1x02_P2.54mm_Vertical, F.Cu at (77.7, 45.4)
- added J3: Conn_01x02, Connector_PinHeader_2.54mm:PinHeader_1x02_P2.54mm_Vertical, F.Cu at (48.5, 45.4)
- added J3: Conn_01x02, Connector_PinHeader_2.54mm:PinHeader_1x02_P2.54mm_Vertical, F.Cu at (106.9, 87.4)
- added J3: Conn_01x02, Connector_PinHeader_2.54mm:PinHeader_1x02_P2.54mm_Vertical, F.Cu at (77.7, 108.4)
- added J3: Conn_01x02, Connector_PinHeader_2.54mm:PinHeader_1x02_P2.54mm_Vertical, F.Cu at (77.7, 118.9)
- added J3: Conn_01x02, Connector_PinHeader_2.54mm:PinHeader_1x02_P2.54mm_Vertical, F.Cu at (48.5, 66.4)
- added J3: Conn_01x02, Connector_PinHeader_2.54mm:PinHeader_1x02_P2.54mm_Vertical, F.Cu at (106.9, 129.4)
- added J3: Conn_01x02, Connector_PinHeader_2.54mm:PinHeader_1x02_P2.54mm_Vertical, F.Cu at (106.9, 66.4)
- added J3: Conn_01x02, Connector_PinHeader_2.54mm:PinHeader_1x02_P2.54mm_Vertical, F.Cu at (48.5, 97.9)
- added J3: Conn_01x02, Connector_PinHeader_2.54mm:PinHeader_1x02_P2.54mm_Vertical, F.Cu at (48.5, 129.4)
- added J3: Conn_01x02, Connector_PinHeader_2.54mm:PinHeader_1x02_P2.54mm_Vertical, F.Cu at (106.9, 118.9)
- added J3: Conn_01x02, Connector_PinHeader_2.54mm:PinHeader_1x02_P2.54mm_Vertical, F.Cu at (106.9, 45.4)
- added J3: Conn_01x02, Connector_PinHeader_2.54mm:PinHeader_1x02_P2.54mm_Vertical, F.Cu at (77.7, 55.9)
- added J3: Conn_01x02, Connector_PinHeader_2.54mm:PinHeader_1x02_P2.54mm_Vertical, F.Cu at (48.5, 108.4)
- added J3: Conn_01x02, Connector_PinHeader_2.54mm:PinHeader_1x02_P2.54mm_Vertical, F.Cu at (77.7, 129.4)
- added J3: Conn_01x02, Connector_PinHeader_2.54mm:PinHeader_1x02_P2.54mm_Vertical, F.Cu at (48.5, 55.9)
- added J3: Conn_01x02, Connector_PinHeader_2.54mm:PinHeader_1x02_P2.54mm_Vertical, F.Cu at (106.9, 97.9)
- added J3: Conn_01x02, Connector_PinHeader_2.54mm:PinHeader_1x02_P2.54mm_Vertical, F.Cu at (77.7, 66.4)
- added J3: Conn_01x02, Connector_PinHeader_2.54mm:PinHeader_1x02_P2.54mm_Vertical, F.Cu at (106.9, 55.9)
- added J4: Conn_01x02, Connector_PinHeader_2.54mm:PinHeader_1x02_P2.54mm_Vertical, F.Cu at (132.5, 97.9)
- added J4: Conn_01x02, Connector_PinHeader_2.54mm:PinHeader_1x02_P2.54mm_Vertical, F.Cu at (132.5, 87.4)
- added J4: Conn_01x02, Connector_PinHeader_2.54mm:PinHeader_1x02_P2.54mm_Vertical, F.Cu at (103.3, 108.4)
- added J4: Conn_01x02, Connector_PinHeader_2.54mm:PinHeader_1x02_P2.54mm_Vertical, F.Cu at (103.3, 55.9)
- added J4: Conn_01x02, Connector_PinHeader_2.54mm:PinHeader_1x02_P2.54mm_Vertical, F.Cu at (132.5, 108.4)
- added J4: Conn_01x02, Connector_PinHeader_2.54mm:PinHeader_1x02_P2.54mm_Vertical, F.Cu at (132.5, 66.4)
- added J4: Conn_01x02, Connector_PinHeader_2.54mm:PinHeader_1x02_P2.54mm_Vertical, F.Cu at (103.3, 45.4)
- added J4: Conn_01x02, Connector_PinHeader_2.54mm:PinHeader_1x02_P2.54mm_Vertical, F.Cu at (74.1, 66.4)
- added J4: Conn_01x02, Connector_PinHeader_2.54mm:PinHeader_1x02_P2.54mm_Vertical, F.Cu at (103.3, 129.4)
- added J4: Conn_01x02, Connector_PinHeader_2.54mm:PinHeader_1x02_P2.54mm_Vertical, F.Cu at (132.5, 45.4)
- added J4: Conn_01x02, Connector_PinHeader_2.54mm:PinHeader_1x02_P2.54mm_Vertical, F.Cu at (74.1, 108.4)
- added J4: Conn_01x02, Connector_PinHeader_2.54mm:PinHeader_1x02_P2.54mm_Vertical, F.Cu at (103.3, 97.9)
- added J4: Conn_01x02, Connector_PinHeader_2.54mm:PinHeader_1x02_P2.54mm_Vertical, F.Cu at (74.1, 97.9)
- added J4: Conn_01x02, Connector_PinHeader_2.54mm:PinHeader_1x02_P2.54mm_Vertical, F.Cu at (74.1, 129.4)
- added J4: Conn_01x02, Connector_PinHeader_2.54mm:PinHeader_1x02_P2.54mm_Vertical, F.Cu at (103.3, 87.4)
- added J4: Conn_01x02, Connector_PinHeader_2.54mm:PinHeader_1x02_P2.54mm_Vertical, F.Cu at (103.3, 118.9)
- added J4: Conn_01x02, Connector_PinHeader_2.54mm:PinHeader_1x02_P2.54mm_Vertical, F.Cu at (132.5, 129.4)
- added J4: Conn_01x02, Connector_PinHeader_2.54mm:PinHeader_1x02_P2.54mm_Vertical, F.Cu at (132.5, 118.9)
- added J4: Conn_01x02, Connector_PinHeader_2.54mm:PinHeader_1x02_P2.54mm_Vertical, F.Cu at (132.5, 55.9)
- added J4: Conn_01x02, Connector_PinHeader_2.54mm:PinHeader_1x02_P2.54mm_Vertical, F.Cu at (74.1, 55.9)
- added J4: Conn_01x02, Connector_PinHeader_2.54mm:PinHeader_1x02_P2.54mm_Vertical, F.Cu at (74.1, 76.9)
- added J4: Conn_01x02, Connector_PinHeader_2.54mm:PinHeader_1x02_P2.54mm_Vertical, F.Cu at (103.3, 76.9)
- added J4: Conn_01x02, Connector_PinHeader_2.54mm:PinHeader_1x02_P2.54mm_Vertical, F.Cu at (74.1, 45.4)
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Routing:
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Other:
- board size 87.6 x 84 mm -> 87.6 x 94.5 mm
